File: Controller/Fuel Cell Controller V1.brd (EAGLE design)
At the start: 160 x 100 mm, 34 parts, among them U1 ATMEGA328P_TQFP, U2 MAX3221CPWR

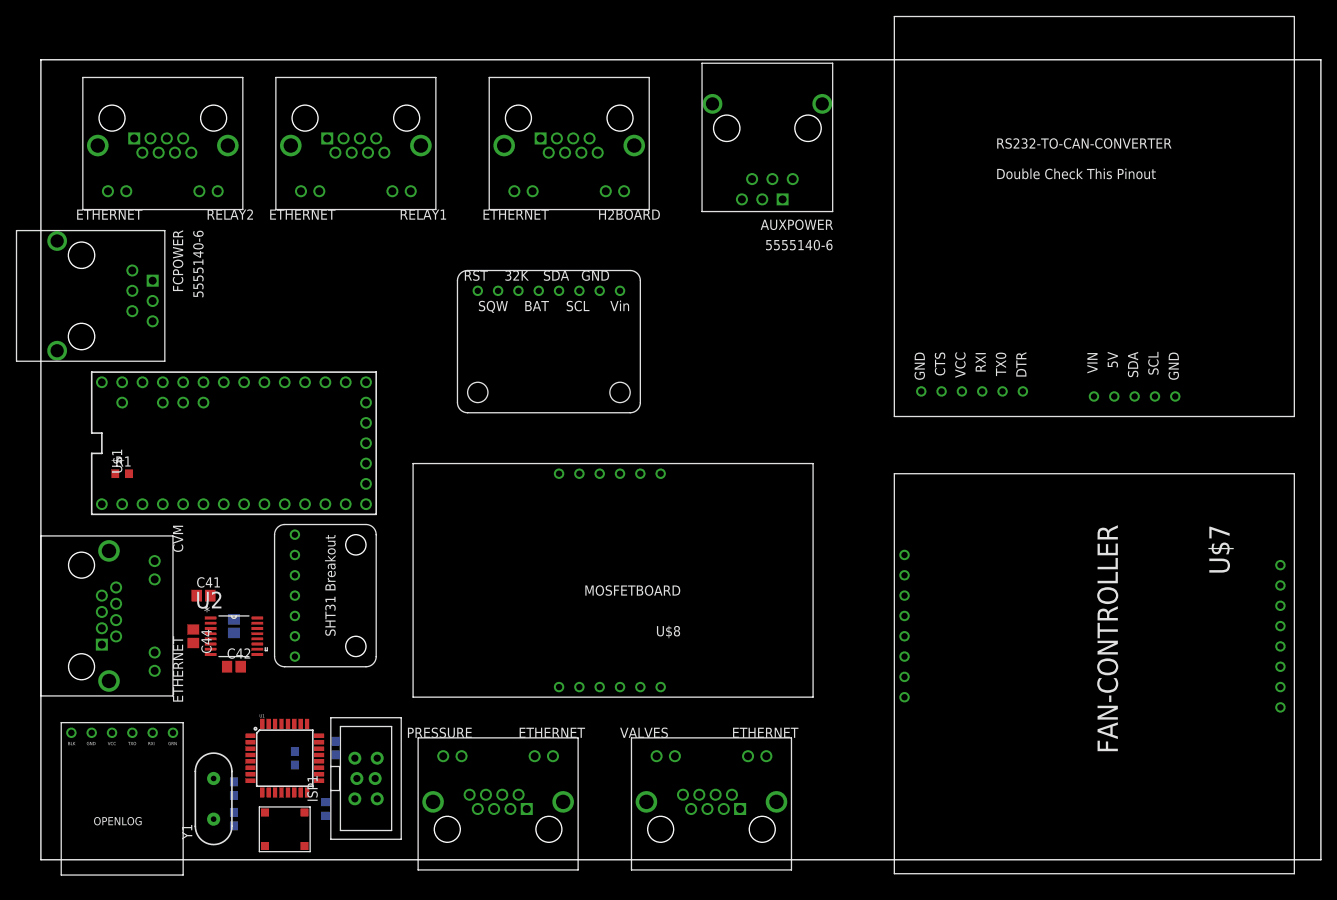
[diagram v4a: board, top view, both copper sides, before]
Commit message: fcc schematic mostly done
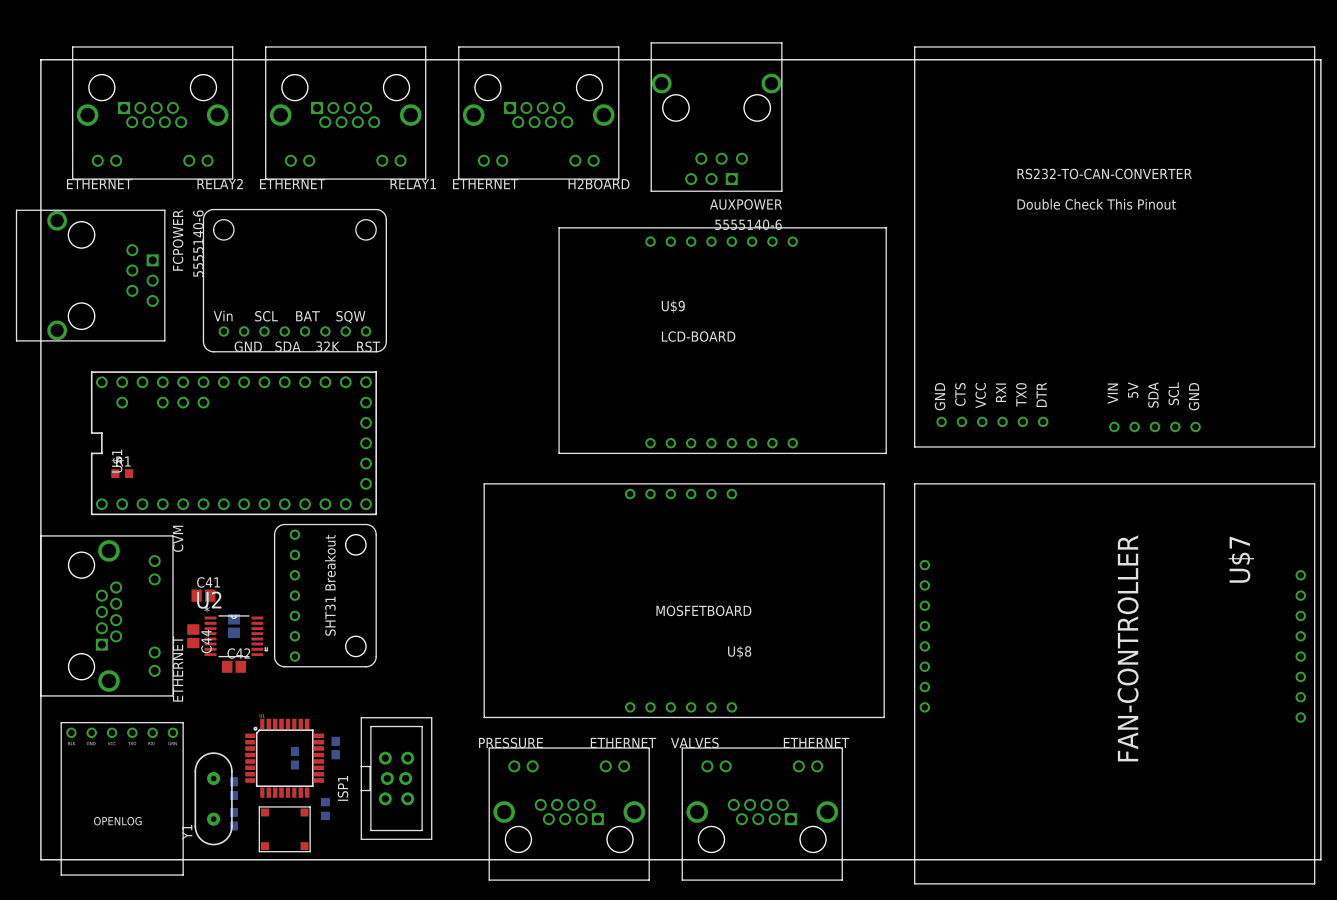
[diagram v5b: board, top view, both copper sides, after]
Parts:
- added FRAME5, FRAME6: FRAME-LETTERNO_PACKAGE, SparkFun-Aesthetics:DUMMY
- added U$9: LCD-BOARD, lcd board:LCD-BOARD
- moved U$4 55.5 mm to (20.3, 63.5), turned to 0 degrees
- moved U$8 9.25 mm to (105.4, 47.0)
- moved PRESSURE 8.98 mm to (66.0, 2.54)
- moved AUXPOWER 6.84 mm to (83.8, 87.6)
- moved VALVES 6.48 mm to (90.2, 2.54)
- moved H2BOARD 5.39 mm to (62.2, 96.5)
- moved U$5 4.58 mm to (109.2, 101.6)
- moved RELAY2 4.02 mm to (14.0, 96.5)
- moved RELAY1 4.02 mm to (38.1, 96.5)
- moved ISP1 3.81 mm to (44.5, 10.2)
- moved U$7 2.84 mm to (109.2, 47.0)
- moved FCPOWER 2.54 mm to (11.4, 72.4)
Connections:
- net +3.3V: now also U$5.VIN, U$9.V
- net GND: now also U$9.GND1, U$9.GND10, U$9.GND11, U$9.GND12, U$9.GND13, U$9.GND2, U$9.GND3, U$9.GND4, U$9.GND5, U$9.GND6, U$9.GND7, U$9.GND8, U$9.GND9
- net SCL: now also U$9.SCL
- net SDA: now also U$9.SDA

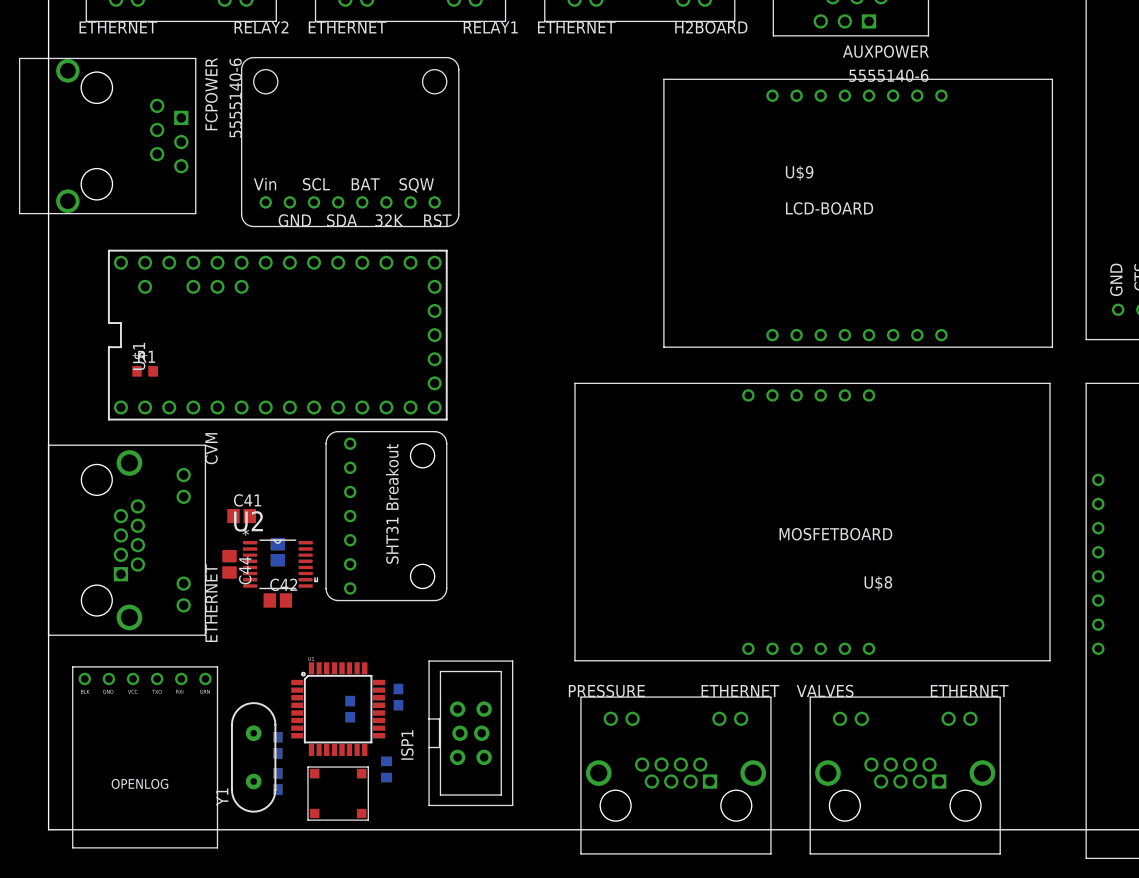
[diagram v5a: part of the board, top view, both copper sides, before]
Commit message: added connector for motor
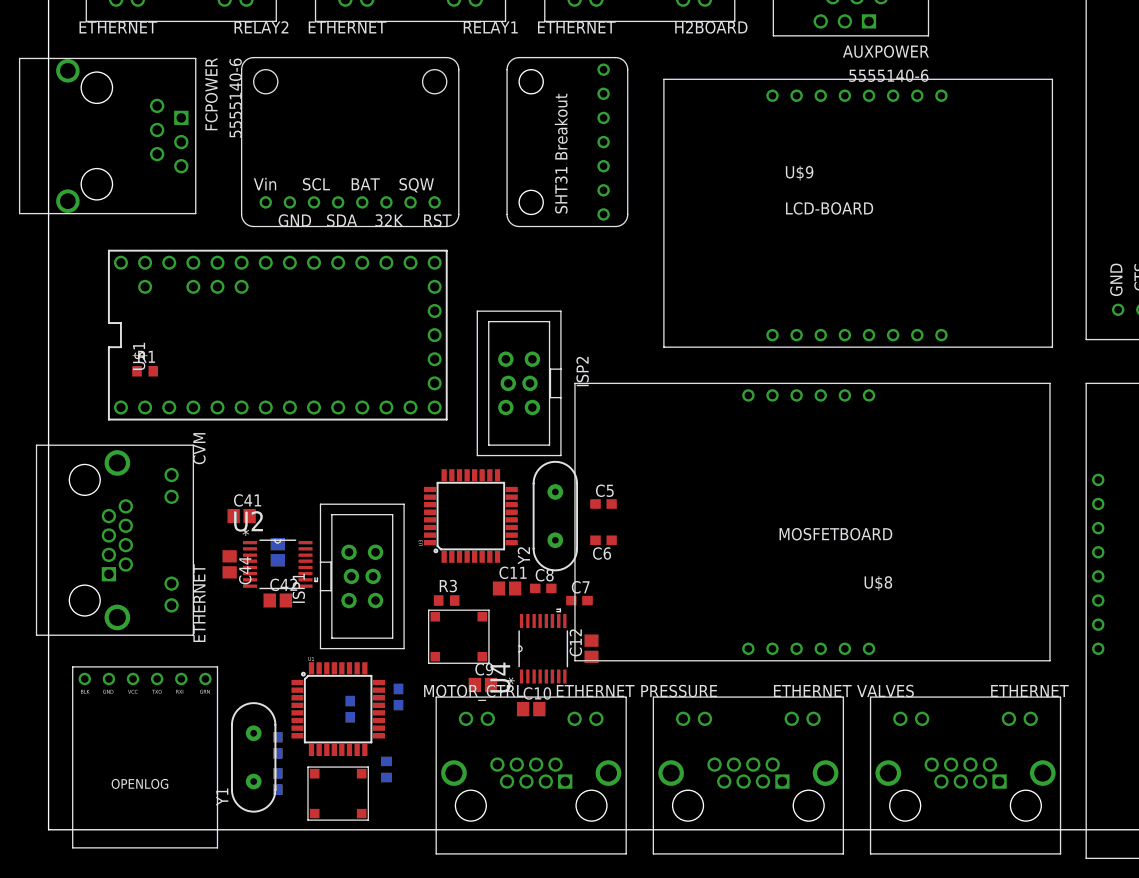
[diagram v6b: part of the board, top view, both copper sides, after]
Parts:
- added C10, C11, C12: 0.33uF/12V, E-P-008-R1.2:C0805
- added C5, C6, C7, C8: (no value), adafruit:C0603
- added C9: 0.047uF/12V, E-P-008-R1.2:C0805
- added ISP2: AVRISP-BOX, adafruit:AVRISP-BOX
- added MOTOR_CTRL: ETHERNET, ETHERNET:A122645-ND
- added R3: (no value), adafruit:R0603
- added U$10: EG4621CT-ND, EG4621CT-ND:EG4621CT-ND
- added U3: ATMEGA328P_TQFP, SparkFun-DigitalIC:TQFP32-08
- added U4: MAX3221CPWR, Texas Instruments_By_element14_Batch_1:SOP65P640X120-16N
- added Y2: (no value), SparkFun-FreqCtrl:HC49US
- moved FRAME5 179.4 mm to (-3.81, 6.35)
- moved FRAME6 176.9 mm to (-3.81, 2.54)
- moved FRAME4 170.8 mm to (-2.54, -1.27)
- moved FRAME3 129.8 mm to (-6.35, -1.27)
- moved FRAME2 126.1 mm to (-3.81, -3.81)
- moved FRAME1 58.9 mm to (-6.35, -1.27)
- moved U$3 38.4 mm to (61.0, 63.5), turned to 90 degrees
- moved ISP1 20.1 mm to (33.0, 26.7)
- moved PRESSURE 7.62 mm to (73.7, 2.54)
- moved VALVES 6.35 mm to (96.5, 2.54)
- moved CVM 1.27 mm to (3.81, 30.5)
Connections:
- net ATMEG_RESET renamed ATMEG1_RESET
- net MISO renamed MISO1
- net MOSI renamed MOSI1
- net RX12 renamed CVMRX12
- net SCK renamed SCK1
- net TX12 renamed CVMTX12
- removed net SER_INVALID: U2.10
- new net ATMEG2_RESET: ISP2.5, R3.1, U$10.P$3, U$10.P$4, U3.29
- new net CVM_SER_INVALID: U1.1, U2.10
- new net GND1: ISP1.6
- new net MISO2: ISP2.1, U3.16
- new net MOSI2: ISP2.4, U3.15
- new net MRX: U3.30, U4.9
- new net MRX12: MOTOR_CTRL.P$2, U4.8
- new net MTX: U3.31, U4.11
- new net MTX12: MOTOR_CTRL.P$1, U4.13
- new net M_SER_INVALID: U3.1, U4.10
- new net N$1: C5.1, U3.7, Y2.2
- new net N$10: C12.1, U4.7
- new net N$2: C6.1, U3.8, Y2.1
- new net N$3: C11.1, U4.3
- new net N$6: C9.1, U4.2
- new net N$7: C9.2, U4.4
- new net N$8: C10.1, U4.5
- new net N$9: C10.2, U4.6
- new net SCK2: ISP2.3, U3.17
- net +3.3V: now also C7.1, C8.1, R3.2, U3.18, U3.20, U3.4, U3.6, U4.15
- net GND: now also C11.2, C12.2, C5.2, C6.2, C7.2, C8.2, ISP2.6, MOTOR_CTRL.P$13, MOTOR_CTRL.P$14, MOTOR_CTRL.P$8, U$10.P$1, U$10.P$2, U3.21, U3.3, U3.5, U4.1, U4.12, U4.14; no longer ISP1.6
- net SCL: now also U3.28
- net SDA: now also U3.27
- net V+: now also U4.16
- net VCC: now also ISP2.2

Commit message: update
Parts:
- added F1, F10, F2, F3, F4, F5, F6, F7, F8, F9: (no value), polyfuse:1206
- added IC1: 4081D, 40xx:SO14
- added SJ1, SJ2: JUMPER-PAD-2-NC_BY_PASTE, SparkFun-Passives:PAD-JUMPER-2-NC_BY_PASTE_YES_SILK
- moved U$4 24.3 mm to (44.5, 61.0), turned to 90 degrees
- moved FRAME2 6.84 mm to (-1.27, 2.54)
- moved FRAME1 6.35 mm to (-1.27, 2.54)
- moved FRAME3 6.35 mm to (-1.27, 2.54)
- moved FRAME5 4.58 mm to (-1.27, 2.54)
- moved FRAME4 3.59 mm to (0.00, 1.27)
- moved FRAME6 2.54 mm to (-1.27, 2.54)
- moved U$1 1.27 mm to (24.1, 50.8)
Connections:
- new net CAP_R_OUT: IC1.10, RELAY1.P$3
- new net CHARGE_R_OUT: IC1.11, RELAY1.P$4
- new net MOTOR_R_OUT: IC1.4, RELAY1.P$2
- new net N$11: F1.2, H2BOARD.P$6
- new net N$12: F2.2, H2BOARD.P$8
- new net N$13: F3.2, U$7.5, U$7.5_2
- new net N$14: F4.2, U$7.12, U$7.12_2, U$7.12_3
- new net N$15: AUXPOWER.1, AUXPOWER.2, F5.2
- new net N$23: F6.1, U$1.VIN
- new net N$24: F7.2, FCPOWER.1, FCPOWER.2
- new net N$25: F8.2, FCPOWER.3, FCPOWER.4
- new net N$26: F9.1, U$1.3.3V, U$1.3.3V1
- new net N$27: CVM.P$1, F10.2
- new net START_R_OUT: IC1.3, RELAY1.P$1
- new net VDD: IC1.14, SJ2.2
- new net VSS: IC1.7, SJ1.2
- net +3.3V: now also F9.2, SJ2.1; no longer U$1.3.3V, U$1.3.3V1
- net AUX12: now also F1.1, F5.1; no longer AUXPOWER.1, AUXPOWER.2, H2BOARD.P$6
- net AUX5: now also F2.1; no longer H2BOARD.P$8
- net CAP_R: now also IC1.8; no longer RELAY1.P$3
- net CHARGE_R: now also IC1.12; no longer RELAY1.P$4
- net EXTRA_SIG: now also U$1.5
- net FC12: now also F4.1, F7.1; no longer FCPOWER.1, FCPOWER.2, U$7.12, U$7.12_2, U$7.12_3
- net FC5: now also F10.1, F3.1, F6.2, F8.1; no longer CVM.P$1, FCPOWER.3, FCPOWER.4, U$1.VIN, U$7.5, U$7.5_2
- net GND: now also SJ1.1
- net H2_OK: now also IC1.13, IC1.2, IC1.6, IC1.9
- net MOTOR_R: now also IC1.5; no longer RELAY1.P$2
- net START_R: now also IC1.1; no longer RELAY1.P$1

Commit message: update
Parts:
- removed C41, C42, C44: 0.33uF/12V, E-P-008-R1.2:C0805
- removed C43: 0.047uF/12V, E-P-008-R1.2:C0805
- removed U$6: EG4621CT-ND, EG4621CT-ND:EG4621CT-ND
- added C13, C14, C15: 0.33uF/12V, E-P-008-R1.2:C0805
- added C16: 0.047uF/12V, E-P-008-R1.2:C0805
- added LED1, LED2, LED3, LED4, LED5, LED6, LED7, LED8: (no value), adafruit:CHIPLED_0805
- added R10, R11, R12, R13, R15, R16, R17, R18, R19: 10k, SparkFun-Resistors:0805
- added R14, R9: (no value), adafruit:R0603
- added R20, R21: 10k, adafruit:R0603
- added R22, R23, R24, R25, R26, R27, R28, R29: (no value), SparkFun-Resistors:0805
- added R4: 4.7k, SparkFun-Resistors:0805
- added R5, R6, R7, R8: 1M, SparkFun-Resistors:0805
- added S1: EG4621CT-ND, EG4621CT-ND:EG4621CT-ND
- added U5: MAX3221CPWR, Texas Instruments_By_element14_Batch_1:SOP65P640X120-16N
- added U6: SN74HC4040D, Texas Instruments_By_element14_Batch_1:SOIC127P600X175-16N
- C1, C3, C4: value (none) -> 0.33uF/12V; device adafruit:C0603 -> E-P-008-R1.2:C0805
- C10, C11, C12: value 0.33uF/12V -> (none); device E-P-008-R1.2:C0805 -> adafruit:C0603
- C6: value (none) -> 0.047uF/12V; device adafruit:C0603 -> E-P-008-R1.2:C0805
- C9: value 0.047uF/12V -> (none); device E-P-008-R1.2:C0805 -> adafruit:C0603
- R1: device adafruit:R0603 -> SparkFun-Resistors:0805
- R2: value (none) -> 10k; device adafruit:R0603 -> SparkFun-Resistors:0805
- R3: value (none) -> 4.7k; device adafruit:R0603 -> SparkFun-Resistors:0805
- U1: value ATMEGA328P_TQFP -> SN74ALS153D; device SparkFun-DigitalIC:TQFP32-08 -> Texas Instruments_By_element14_Batch_1:SOIC127P600X175-16N
- U4: value MAX3221CPWR -> ATMEGA328P_TQFP; device Texas Instruments_By_element14_Batch_1:SOP65P640X120-16N -> SparkFun-DigitalIC:TQFP32-08
- moved F3 138.7 mm to (14.0, 29.2), flipped to the bottom
- moved F10 130.6 mm to (74.9, 81.3), turned to 180 degrees
- moved F9 119.4 mm to (64.8, 81.3), turned to 180 degrees
- moved F7 103.4 mm to (106.0, 17.8), turned to 0 degrees
- moved F8 96.6 mm to (106.0, 27.9), turned to 0 degrees
- moved F4 87.9 mm to (82.5, 81.3)
- moved F6 80.7 mm to (19.1, 69.8), turned to 180 degrees
- moved F2 66.7 mm to (8.89, 62.2), turned to 0 degrees
- moved F5 62.6 mm to (19.1, 74.9), turned to 180 degrees
- moved F1 47.6 mm to (19.1, 65.4), turned to 0 degrees
- moved R2 44.9 mm to (15.2, 46.4), flipped to the top, turned to 270 degrees
- moved C7 35.2 mm to (24.1, 8.89), flipped to the bottom, turned to 270 degrees
- moved R3 34.7 mm to (25.4, 54.6), turned to 90 degrees
- moved C8 34.5 mm to (24.1, 5.08), flipped to the bottom, turned to 270 degrees
- moved C6 34.3 mm to (24.1, 29.2), flipped to the bottom, turned to 270 degrees
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- renumbered AUXPOWER to E1, CVM to ETH3, FCPOWER to E2, H2BOARD to ETH7, MOTOR_CTRL to ETH4, PRESSURE to ETH5, RELAY1 to ETH1, RELAY2 to ETH2, U$1 to T1, U$10 to S2, U$2 to O1, U$3 to SHT1, U$4 to RTC1, U$5 to CAN1, U$7 to FAN1, U$8 to M1, U$9 to LCD1, VALVES to ETH6
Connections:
- new net LED_CLK: T1.13, U6.10
- new net MULTA: T1.3, U1.14
- new net MULTB: T1.4, U1.2
- new net MULTO1: R1.1, T1.5, U1.7
- new net MULTO2: R2.2, T1.2, U1.9
- new net M_SIG_1: ETH4.P$6, U1.12
- new net M_SIG_2: ETH4.P$7, U1.13
- new net N$28: R24.2, U6.6
- new net N$29: R25.2, U6.5
- new net N$30: R26.2, U6.3
- new net N$31: R27.2, U6.2
- new net N$32: R28.2, U6.4
- new net N$33: R29.2, U6.13
- new net N$34: U6.11, U6.12
- new net N$35: LED5.A, R26.1
- new net N$36: LED6.A, R27.1
- new net N$37: LED7.A, R28.1
- new net N$38: LED8.A, R29.1
- net +3.3V: now also C10.1, C2.1, C5.1, C9.1, F1.2, R14.2, R3.1, R4.1, R5.2, R6.2, R9.2, U4.18, U4.20, U4.4, U4.6, U5.15, U6.16; no longer C3.1, C4.1, C7.1, C8.1, F9.2, R2.2, R3.2, U1.18, U1.20, U1.4, U1.6, U4.15
- net ATMEG1_RESET: now also R9.1, S1.P$3, S1.P$4, U3.29; no longer R2.1, U$6.P$3, U$6.P$4, U1.29
- net ATMEG2_RESET: now also R14.1, U4.29; no longer R3.1, U3.29
- net AUX12: now also F4.1, F9.1; no longer F1.1, F5.1
- net AUX5: now also F10.1; no longer F2.1
- net CAPCURR: now also R5.1
- net CAPVOLT: now also R7.1
- net CVMRX: now also U3.30; no longer U1.30
- net CVMSIG1: now also R13.2, U1.6
- net CVMSIG2: now also R12.2, U1.5
- net CVMSIG3: now also R11.2, U1.4
- net CVMSIG4: now also R10.2, U1.3
- net CVMTX: now also U3.31; no longer U1.31
- net CVM_SER_INVALID: now also U3.1; no longer U1.1
- net EXTRA_SIG: now also R21.2, U1.11; no longer T1.5
- net EXTRA_V_G: now also R15.2
- net FC12: now also F5.1, F8.1; no longer F4.1, F7.1
- net FC5: now also F2.2, F6.1, F7.1, U1.16; no longer F10.1, F6.2, F8.1
- net FCCURR: now also R6.1
- net FCPRES: now also R19.1
- net FCVOLT: now also R8.1
- net GND: now also C10.2, C14.2, C15.2, C9.2, ETH5.P$13, ETH5.P$14, LED1.C, LED2.C, LED3.C, LED4.C, LED5.C, LED6.C, LED7.C, LED8.C, R1.2, R10.1, R11.1, R12.1, R13.1, R15.1, R16.1, R17.1, R18.1, R2.1, R20.1, R21.1, R7.2, R8.2, S1.P$1, S1.P$2, U1.1, U1.15, U1.8, U4.21, U4.3, U4.5, U5.1, U5.12, U5.14, U6.8; no longer C1.2, C41.2, C42.2, C6.2, R1.1, U$6.P$1, U$6.P$2, U1.21, U1.3, U1.5, U4.1, U4.12, U4.14
- net H2_OK: now also R20.2, U1.10; no longer R1.2, T1.2
- net MISO1: now also U3.16; no longer U1.16
- net MISO2: now also U4.16; no longer U3.16
- net MOSI1: now also U3.15; no longer U1.15
- net MOSI2: now also U4.15; no longer U3.15
- net MRX: now also U4.30, U5.9; no longer U3.30, U4.9
- net MRX12: now also U5.8; no longer U4.8
- net MTX: now also U4.31, U5.11; no longer U3.31, U4.11
- net MTX12: now also U5.13; no longer U4.13
- net M_SER_INVALID: now also U4.1, U5.10; no longer U3.1, U4.10
- net N$1: now also C11.1, U4.7; no longer C5.1, U3.7
- net N$10: now also C15.1, U5.7; no longer C12.1, U4.7
- net N$11: now also F9.2; no longer F1.2
- net N$12: now also F10.2; no longer F2.2
- net N$13: now also F7.2; no longer F3.2
- net N$14: now also F8.2; no longer F4.2
- net N$15: now also F4.2; no longer F5.2
- net N$16: now also LED1.A, R22.1; no longer ETH5.P$4
- net N$17: now also R18.2, R19.2; no longer ETH5.P$5
- net N$18: now also LED2.A, R23.1; no longer ETH5.P$6
- net N$19: now also LED3.A, R24.1; no longer ETH5.P$7
- net N$2: now also C12.1, U4.8; no longer C6.1, U3.8
- net N$20: now also LED4.A, R25.1; no longer ETH5.P$8
- net N$21: now also R22.2, U6.9; no longer ETH5.P$13
- net N$22: now also R23.2, U6.7; no longer ETH5.P$14
- net N$23: now also F2.1; no longer F6.1
- net N$24: now also F5.2; no longer F7.2
- net N$25: now also F6.2; no longer F8.2
- net N$26: now also F1.1; no longer F9.1
- net N$27: now also F3.2; no longer F10.2
- net N$3: now also C14.1, U5.3; no longer C11.1, U4.3
- net N$4: now also C7.1, U3.7; no longer C1.1, U1.7
- net N$5: now also C8.1, U3.8; no longer C2.1, U1.8
- net N$6: now also C16.1, U5.2; no longer C9.1, U4.2
- net N$7: now also C16.2, U5.4; no longer C9.2, U4.4
- net N$73: now also C3.1; no longer C41.1
- net N$74: now also C6.1; no longer C43.1
- net N$75: now also C6.2; no longer C43.2
- net N$76: now also C1.1; no longer C44.1
- net N$77: now also C1.2; no longer C44.2
- net N$78: now also C4.1; no longer C42.1
- net N$8: now also C13.1, U5.5; no longer C10.1, U4.5
- net N$9: now also C13.2, U5.6; no longer C10.2, U4.6
- net PURGE_V_G: now also R16.2
- net SCK1: now also U3.17; no longer U1.17
- net SCK2: now also U4.17; no longer U3.17
- net SCL: now also R3.2, U4.28; no longer U1.28
- net SDA: now also R4.2, U4.27; no longer U1.27
- net SUPPLY_V_G: now also R17.2
- net V+: now also U5.16; no longer U4.16
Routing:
- added copper zone on layer 1, net GND
- added copper zone on layer 16, net GND
